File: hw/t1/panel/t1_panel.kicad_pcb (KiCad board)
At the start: 4 copper layers, 70.5 x 81 mm, 376 parts, among them J1 SFP edge (INF-8074i), J2 Rosenberger E6S20A-40MT5-Z (H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, U1 DP83TG720S-Q1 (or DP83TC812S-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, U2 STM32G031F6P6, U3 TPS62822DLC, Y1 25MHz CL8pF 2016

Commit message: t1: opens clean in KiCad 9 - schematic parity, linked footprints, check script
A KiCad 9 check (official Docker image, as a reviewer would open it) found
what KiCad 7's python and kicad-cli could not test:
- no footprint was linked to its schematic symbol: KiCad's Update PCB
  would have replaced every part. Footprints now carry /<symbol uuid>
  plus Sheetname/Sheetfile
- 140 net-name conflicts: local labels name nets /TD_P on the root sheet,
  the board says TD_P. The schematic now uses global labels
- no-connect pins are nets of their own in KiCad
  (unconnected-(REF-PIN-PadN)); the pads now carry them
- DNP/BOM flags agreed nowhere (ESD diodes, test pads): excluded from the
  BOM on both sides (KiCad 7 boards have no DNP attribute)
- back-side label was not mirrored
- the buck's footprint is gone from KiCad 9's library: vendored into
  hw/fp/sfp.pretty

Result (sh hw/check_kicad9.sh t1): DRC 0 errors / 0 unconnected, parity
clean, ERC 0 errors; the only warnings are KiCad 9's newer library copies.
Copper is unchanged (tracks, vias, pads and fills compared item by item);
gerber/CPL/BOM changes are ordering only. KiCad 7 ERC 0/0, DRC 0/0.
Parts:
- removed the U3 at (125.2, 59.3)
- removed the U3 at (125.2, 45.5)
- removed the U3 at (125.2, 31.7)
- removed the U3 at (125.2, 86.9)
- removed the U3 at (125.2, 73.1)
- added U3: TPS62822DLC, sfp:Texas_VSON-HR-8_1.5x2mm_P0.5mm, F.Cu at (125.2, 45.5)
- added U3: TPS62822DLC, sfp:Texas_VSON-HR-8_1.5x2mm_P0.5mm, F.Cu at (125.2, 59.3)
- added U3: TPS62822DLC, sfp:Texas_VSON-HR-8_1.5x2mm_P0.5mm, F.Cu at (125.2, 73.1)
- added U3: TPS62822DLC, sfp:Texas_VSON-HR-8_1.5x2mm_P0.5mm, F.Cu at (125.2, 86.9)
- added U3: TPS62822DLC, sfp:Texas_VSON-HR-8_1.5x2mm_P0.5mm, F.Cu at (125.2, 31.7)
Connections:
- J1 pad 7: (no net) -> Board_0-unconnected-(J1-RS0-Pad7)
- J1 pad 7: (no net) -> Board_3-unconnected-(J1-RS0-Pad7)
- J1 pad 7: (no net) -> Board_4-unconnected-(J1-RS0-Pad7)
- J1 pad 7: (no net) -> Board_2-unconnected-(J1-RS0-Pad7)
- J1 pad 7: (no net) -> Board_1-unconnected-(J1-RS0-Pad7)
- U1 pad 10: (no net) -> Board_3-unconnected-(U1-INH-Pad10)
- U1 pad 14: (no net) -> Board_3-unconnected-(U1-STRP_1-Pad14)
- U1 pad 15: (no net) -> Board_3-unconnected-(U1-RX_CTRL-Pad15)
- U1 pad 16: (no net) -> Board_3-unconnected-(U1-CLKOUT-Pad16)
- U1 pad 17: (no net) -> Board_3-unconnected-(U1-DNC-Pad17)
- U1 pad 18: (no net) -> Board_3-unconnected-(U1-DNC-Pad18)
- U1 pad 19: (no net) -> Board_3-unconnected-(U1-DNC-Pad19)
- U1 pad 20: (no net) -> Board_3-unconnected-(U1-DNC-Pad20)
- U1 pad 25: (no net) -> Board_3-unconnected-(U1-RX_D1-Pad25)
- U1 pad 26: (no net) -> Board_3-unconnected-(U1-RX_D0-Pad26)
- U1 pad 27: (no net) -> Board_3-unconnected-(U1-RX_CLK-Pad27)
- U1 pad 28: (no net) -> Board_3-unconnected-(U1-TX_CLK-Pad28)
- U1 pad 29: (no net) -> Board_3-unconnected-(U1-TX_CTRL-Pad29)
- U1 pad 30: (no net) -> Board_3-unconnected-(U1-TX_D3-Pad30)
- U1 pad 31: (no net) -> Board_3-unconnected-(U1-TX_D2-Pad31)
- U1 pad 6: (no net) -> Board_3-unconnected-(U1-LED_1/AUTO-Pad6)
- U1 pad 8: (no net) -> Board_3-unconnected-(U1-WAKE-Pad8)
- U1 pad 10: (no net) -> Board_1-unconnected-(U1-INH-Pad10)
- U1 pad 14: (no net) -> Board_1-unconnected-(U1-STRP_1-Pad14)
- U1 pad 15: (no net) -> Board_1-unconnected-(U1-RX_CTRL-Pad15)
- U1 pad 16: (no net) -> Board_1-unconnected-(U1-CLKOUT-Pad16)
- U1 pad 17: (no net) -> Board_1-unconnected-(U1-DNC-Pad17)
- U1 pad 18: (no net) -> Board_1-unconnected-(U1-DNC-Pad18)
- U1 pad 19: (no net) -> Board_1-unconnected-(U1-DNC-Pad19)
- U1 pad 20: (no net) -> Board_1-unconnected-(U1-DNC-Pad20)
- U1 pad 25: (no net) -> Board_1-unconnected-(U1-RX_D1-Pad25)
- U1 pad 26: (no net) -> Board_1-unconnected-(U1-RX_D0-Pad26)
- U1 pad 27: (no net) -> Board_1-unconnected-(U1-RX_CLK-Pad27)
- U1 pad 28: (no net) -> Board_1-unconnected-(U1-TX_CLK-Pad28)
- U1 pad 29: (no net) -> Board_1-unconnected-(U1-TX_CTRL-Pad29)
- U1 pad 30: (no net) -> Board_1-unconnected-(U1-TX_D3-Pad30)
- U1 pad 31: (no net) -> Board_1-unconnected-(U1-TX_D2-Pad31)
- U1 pad 6: (no net) -> Board_1-unconnected-(U1-LED_1/AUTO-Pad6)
- U1 pad 8: (no net) -> Board_1-unconnected-(U1-WAKE-Pad8)
- U1 pad 10: (no net) -> Board_4-unconnected-(U1-INH-Pad10)
- U1 pad 14: (no net) -> Board_4-unconnected-(U1-STRP_1-Pad14)
- U1 pad 15: (no net) -> Board_4-unconnected-(U1-RX_CTRL-Pad15)
- U1 pad 16: (no net) -> Board_4-unconnected-(U1-CLKOUT-Pad16)
- U1 pad 17: (no net) -> Board_4-unconnected-(U1-DNC-Pad17)
- U1 pad 18: (no net) -> Board_4-unconnected-(U1-DNC-Pad18)
- U1 pad 19: (no net) -> Board_4-unconnected-(U1-DNC-Pad19)
- U1 pad 20: (no net) -> Board_4-unconnected-(U1-DNC-Pad20)
- U1 pad 25: (no net) -> Board_4-unconnected-(U1-RX_D1-Pad25)
- U1 pad 26: (no net) -> Board_4-unconnected-(U1-RX_D0-Pad26)
- U1 pad 27: (no net) -> Board_4-unconnected-(U1-RX_CLK-Pad27)
- U1 pad 28: (no net) -> Board_4-unconnected-(U1-TX_CLK-Pad28)
- U1 pad 29: (no net) -> Board_4-unconnected-(U1-TX_CTRL-Pad29)
- U1 pad 30: (no net) -> Board_4-unconnected-(U1-TX_D3-Pad30)
- U1 pad 31: (no net) -> Board_4-unconnected-(U1-TX_D2-Pad31)
- U1 pad 6: (no net) -> Board_4-unconnected-(U1-LED_1/AUTO-Pad6)
- U1 pad 8: (no net) -> Board_4-unconnected-(U1-WAKE-Pad8)
- U1 pad 10: (no net) -> Board_0-unconnected-(U1-INH-Pad10)
- U1 pad 14: (no net) -> Board_0-unconnected-(U1-STRP_1-Pad14)
- U1 pad 15: (no net) -> Board_0-unconnected-(U1-RX_CTRL-Pad15)
- U1 pad 16: (no net) -> Board_0-unconnected-(U1-CLKOUT-Pad16)
- U1 pad 17: (no net) -> Board_0-unconnected-(U1-DNC-Pad17)
- U1 pad 18: (no net) -> Board_0-unconnected-(U1-DNC-Pad18)
- U1 pad 19: (no net) -> Board_0-unconnected-(U1-DNC-Pad19)
- U1 pad 20: (no net) -> Board_0-unconnected-(U1-DNC-Pad20)
- U1 pad 25: (no net) -> Board_0-unconnected-(U1-RX_D1-Pad25)
- U1 pad 26: (no net) -> Board_0-unconnected-(U1-RX_D0-Pad26)
- U1 pad 27: (no net) -> Board_0-unconnected-(U1-RX_CLK-Pad27)
- U1 pad 28: (no net) -> Board_0-unconnected-(U1-TX_CLK-Pad28)
- U1 pad 29: (no net) -> Board_0-unconnected-(U1-TX_CTRL-Pad29)
- U1 pad 30: (no net) -> Board_0-unconnected-(U1-TX_D3-Pad30)
- U1 pad 31: (no net) -> Board_0-unconnected-(U1-TX_D2-Pad31)
- U1 pad 6: (no net) -> Board_0-unconnected-(U1-LED_1/AUTO-Pad6)
- U1 pad 8: (no net) -> Board_0-unconnected-(U1-WAKE-Pad8)
- U1 pad 10: (no net) -> Board_2-unconnected-(U1-INH-Pad10)
- U1 pad 14: (no net) -> Board_2-unconnected-(U1-STRP_1-Pad14)
- U1 pad 15: (no net) -> Board_2-unconnected-(U1-RX_CTRL-Pad15)
- U1 pad 16: (no net) -> Board_2-unconnected-(U1-CLKOUT-Pad16)
- U1 pad 17: (no net) -> Board_2-unconnected-(U1-DNC-Pad17)
- U1 pad 18: (no net) -> Board_2-unconnected-(U1-DNC-Pad18)
- U1 pad 19: (no net) -> Board_2-unconnected-(U1-DNC-Pad19)
- U1 pad 20: (no net) -> Board_2-unconnected-(U1-DNC-Pad20)
- U1 pad 25: (no net) -> Board_2-unconnected-(U1-RX_D1-Pad25)
- U1 pad 26: (no net) -> Board_2-unconnected-(U1-RX_D0-Pad26)
- U1 pad 27: (no net) -> Board_2-unconnected-(U1-RX_CLK-Pad27)
- U1 pad 28: (no net) -> Board_2-unconnected-(U1-TX_CLK-Pad28)
- U1 pad 29: (no net) -> Board_2-unconnected-(U1-TX_CTRL-Pad29)
- U1 pad 30: (no net) -> Board_2-unconnected-(U1-TX_D3-Pad30)
- U1 pad 31: (no net) -> Board_2-unconnected-(U1-TX_D2-Pad31)
- U1 pad 6: (no net) -> Board_2-unconnected-(U1-LED_1/AUTO-Pad6)
- U1 pad 8: (no net) -> Board_2-unconnected-(U1-WAKE-Pad8)
- U2 pad 14: (no net) -> Board_0-unconnected-(U2-PA7-Pad14)
- U2 pad 15: (no net) -> Board_0-unconnected-(U2-PB0/PB1/PB2/PA8-Pad15)
- U2 pad 16: (no net) -> Board_0-unconnected-(U2-PA11/PA9-Pad16)
- U2 pad 17: (no net) -> Board_0-unconnected-(U2-PA12/PA10-Pad17)
- U2 pad 2: (no net) -> Board_0-unconnected-(U2-PC14/PB9-Pad2)
- U2 pad 3: (no net) -> Board_0-unconnected-(U2-PC15-Pad3)
- U2 pad 14: (no net) -> Board_4-unconnected-(U2-PA7-Pad14)
- U2 pad 15: (no net) -> Board_4-unconnected-(U2-PB0/PB1/PB2/PA8-Pad15)
- U2 pad 16: (no net) -> Board_4-unconnected-(U2-PA11/PA9-Pad16)
- U2 pad 17: (no net) -> Board_4-unconnected-(U2-PA12/PA10-Pad17)
- U2 pad 2: (no net) -> Board_4-unconnected-(U2-PC14/PB9-Pad2)
- U2 pad 3: (no net) -> Board_4-unconnected-(U2-PC15-Pad3)
- U2 pad 14: (no net) -> Board_2-unconnected-(U2-PA7-Pad14)
- U2 pad 15: (no net) -> Board_2-unconnected-(U2-PB0/PB1/PB2/PA8-Pad15)
- U2 pad 16: (no net) -> Board_2-unconnected-(U2-PA11/PA9-Pad16)
- U2 pad 17: (no net) -> Board_2-unconnected-(U2-PA12/PA10-Pad17)
- U2 pad 2: (no net) -> Board_2-unconnected-(U2-PC14/PB9-Pad2)
- U2 pad 3: (no net) -> Board_2-unconnected-(U2-PC15-Pad3)
- U2 pad 14: (no net) -> Board_3-unconnected-(U2-PA7-Pad14)
- U2 pad 15: (no net) -> Board_3-unconnected-(U2-PB0/PB1/PB2/PA8-Pad15)
- U2 pad 16: (no net) -> Board_3-unconnected-(U2-PA11/PA9-Pad16)
- U2 pad 17: (no net) -> Board_3-unconnected-(U2-PA12/PA10-Pad17)
- U2 pad 2: (no net) -> Board_3-unconnected-(U2-PC14/PB9-Pad2)
- U2 pad 3: (no net) -> Board_3-unconnected-(U2-PC15-Pad3)
- U2 pad 14: (no net) -> Board_1-unconnected-(U2-PA7-Pad14)
- U2 pad 15: (no net) -> Board_1-unconnected-(U2-PB0/PB1/PB2/PA8-Pad15)
- U2 pad 16: (no net) -> Board_1-unconnected-(U2-PA11/PA9-Pad16)
- U2 pad 17: (no net) -> Board_1-unconnected-(U2-PA12/PA10-Pad17)
- U2 pad 2: (no net) -> Board_1-unconnected-(U2-PC14/PB9-Pad2)
- U2 pad 3: (no net) -> Board_1-unconnected-(U2-PC15-Pad3)

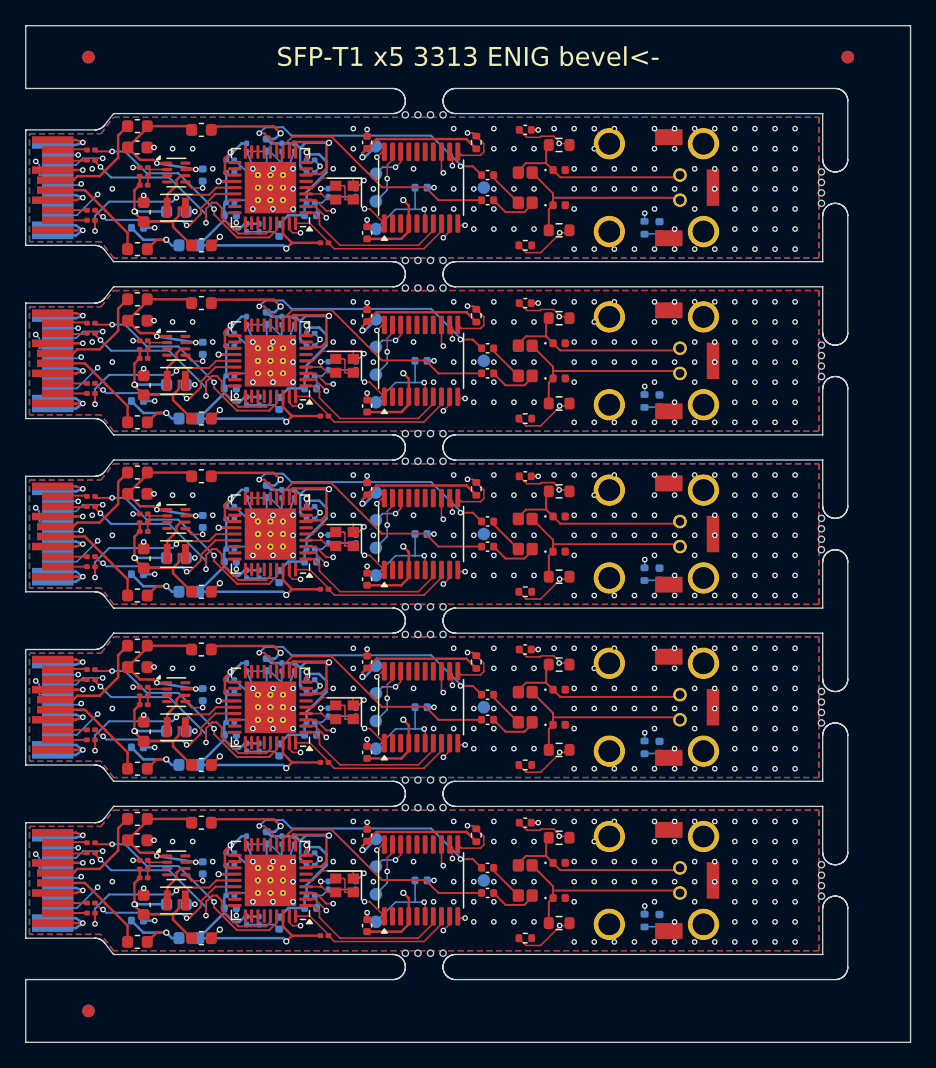
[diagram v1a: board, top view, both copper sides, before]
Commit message: t1: design-review fixes - coupled pairs by hand, F/GND/GND/B, load switch, two BOMs, CI
- every SGMII/MDI pair laid coupled (0.114/0.152, ~100 ohm diff) on one layer
  with matched vias; router does the slow nets only. Worst skew 1.08 mm (SG_RX)
- In2 is GND; slow signals may cross it except under the bottom-side pair
- SGMII lanes laid straight, polarity inverted in the PHY by the firmware
  (SGMII_CTRL_1 bits 7/8, TG720 and TC812)
- TPS22918 load switch on the 3.3 V entry (~3.6 ms soft start)
- 0.6 mm no-copper strip along every edge (mouse bites); escapes where it
  closed the router's way (U4 ON, MDC/INT/RST, VDD1P0, MCU GND, XO)
- jlc/bom.csv + cpl.csv replaced by bom/cpl-tg720 and bom/cpl-tc812
- fab/t1-1to1.pdf for the H-MTD print check
- KiCad 9: DRC 0, parity clean, ERC clean; only lib-revision warnings pass
- GitHub Actions: KiCad 9 check, firmware (4 variants, no warnings), gateware
- root README rewritten (11.8 mm body, current status, hardware-only checks)
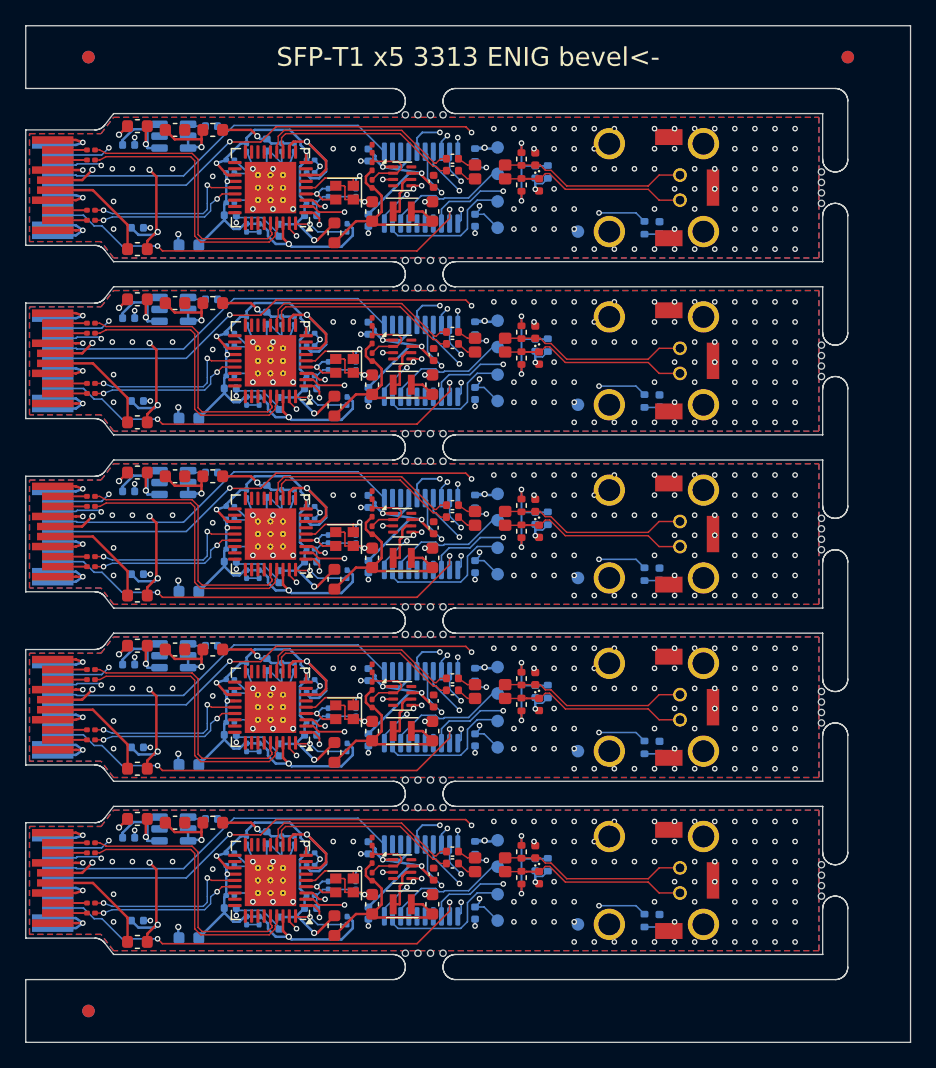
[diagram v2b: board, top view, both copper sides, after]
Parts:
- removed the C1 at (122.2, 43.5)
- removed the C1 at (122.2, 84.9)
- removed the C1 at (122.2, 57.3)
- removed the C1 at (122.2, 29.7)
- removed the C1 at (122.2, 71.1)
- removed the C26 at (127.3, 31.9)
- removed the C26 at (127.3, 45.7)
- removed the C26 at (127.3, 73.3)
- removed the C26 at (127.3, 59.5)
- removed the C26 at (127.3, 87.1)
- removed the C27 at (122.7, 90.0)
- removed the C27 at (122.7, 76.2)
- removed the C27 at (122.7, 34.9)
- removed the C27 at (122.7, 48.6)
- removed the C27 at (122.7, 62.5)
- removed the C28 at (125.2, 62.4)
- removed the C28 at (125.2, 48.6)
- removed the C28 at (125.2, 34.8)
- removed the C28 at (125.2, 76.2)
- removed the C28 at (125.2, 90.0)
- removed the C29 at (122.7, 59.6)
- removed the C29 at (122.7, 73.4)
- removed the C29 at (122.7, 87.2)
- removed the C29 at (122.7, 32.0)
- removed the C29 at (122.7, 45.8)
- removed the C30 at (140.4, 56.9)
- removed the C30 at (140.4, 43.1)
- removed the C30 at (140.4, 29.3)
- removed the C30 at (140.4, 70.7)
- removed the C30 at (140.4, 84.5)
- removed the C31 at (140.4, 50.3)
- removed the C31 at (140.4, 91.7)
- removed the C31 at (140.4, 77.9)
- removed the C31 at (140.4, 64.1)
- removed the C31 at (140.4, 36.5)
- removed the C32 at (144.8, 46.7)
- removed the C32 at (144.8, 88.1)
- removed the C32 at (144.8, 74.3)
- removed the C32 at (144.8, 32.9)
- removed the C32 at (144.8, 60.5)
- removed the C33 at (150.1, 87.1)
- removed the C33 at (150.1, 59.5)
- removed the C33 at (150.1, 73.3)
- removed the C33 at (150.1, 31.9)
- removed the C33 at (150.1, 45.7)
- removed the C34 at (150.1, 33.9)
- removed the C34 at (150.1, 61.5)
- removed the C34 at (150.1, 47.7)
- removed the C34 at (150.1, 89.1)
- removed the C34 at (150.1, 75.3)
- removed the C35 at (153.1, 28.3)
- removed the C35 at (153.1, 83.5)
- removed the C35 at (153.1, 55.9)
- removed the C35 at (153.1, 69.7)
- removed the C35 at (153.1, 42.1)
- removed the D2 at (155.8, 72.9)
- removed the D2 at (155.8, 31.5)
- removed the D2 at (155.8, 86.7)
- removed the D2 at (155.8, 45.3)
- removed the D2 at (155.8, 59.1)
- removed the D3 at (155.8, 75.7)
- removed the D3 at (155.8, 34.3)
- removed the D3 at (155.8, 48.1)
- removed the D3 at (155.8, 89.5)
- removed the D3 at (155.8, 61.9)
- removed the FB3 at (127.2, 37.5)
- removed the FB3 at (127.2, 92.7)
- removed the FB3 at (127.2, 78.9)
- removed the FB3 at (127.2, 51.3)
- removed the FB3 at (127.2, 65.1)
- removed the FB4 at (127.2, 69.7)
- removed the FB4 at (127.2, 55.9)
- removed the FB4 at (127.2, 42.1)
- removed the FB4 at (127.2, 83.5)
- removed the FB4 at (127.2, 28.3)
- removed the L1 at (125.2, 75.9)
- removed the L1 at (125.2, 34.5)
- removed the L1 at (125.2, 62.1)
- removed the L1 at (125.2, 48.3)
- removed the L1 at (125.2, 89.7)
- removed the L2 at (153.1, 60.5)
- removed the L2 at (153.1, 32.9)
- removed the L2 at (153.1, 88.1)
- removed the L2 at (153.1, 74.3)
- removed the L2 at (153.1, 46.7)
- removed the R1 at (137.1, 64.9)
- removed the R1 at (137.1, 78.7)
- removed the R1 at (137.1, 37.3)
- removed the R1 at (137.1, 51.1)
- removed the R1 at (137.1, 92.5)
- removed the R3 at (122.7, 87.9)
- removed the R3 at (122.7, 74.1)
- removed the R3 at (122.7, 46.5)
- removed the R3 at (122.7, 60.3)
- removed the R3 at (122.7, 32.7)
- removed the R4 at (122.7, 72.7)
- removed the R4 at (122.7, 86.5)
- removed the R4 at (122.7, 58.9)
- removed the R4 at (122.7, 31.3)
- removed the R4 at (122.7, 45.1)
- removed the R5 at (149.2, 29.3)
- removed the R5 at (149.2, 56.9)
- removed the R5 at (149.2, 70.7)
- removed the R5 at (149.2, 43.1)
- removed the R5 at (149.2, 84.5)
- removed the R6 at (155.8, 57.1)
- removed the R6 at (155.8, 43.3)
- removed the R6 at (155.8, 84.7)
- removed the R6 at (155.8, 70.9)
- removed the R6 at (155.8, 29.5)
- removed the R7 at (155.8, 91.5)
- removed the R7 at (155.8, 50.1)
- removed the R7 at (155.8, 36.3)
- removed the R7 at (155.8, 77.7)
- removed the R7 at (155.8, 63.9)
- removed the R8 at (153.1, 37.5)
- removed the R8 at (153.1, 78.9)
- removed the R8 at (153.1, 65.1)
- removed the R8 at (153.1, 92.7)
- removed the R8 at (153.1, 51.3)
- removed the TP1 at (141.2, 43.4)
- removed the TP1 at (141.2, 57.2)
- removed the TP1 at (141.2, 84.8)
- removed the TP1 at (141.2, 29.6)
- removed the TP1 at (141.2, 71.0)
- removed the TP2 at (141.2, 31.8)
- removed the TP2 at (141.2, 73.2)
- removed the TP2 at (141.2, 59.4)
- removed the TP2 at (141.2, 45.6)
- removed the TP2 at (141.2, 87.0)
- removed the TP3 at (141.2, 75.4)
- removed the TP3 at (141.2, 34.0)
- removed the TP3 at (141.2, 89.2)
- removed the TP3 at (141.2, 61.6)
- removed the TP3 at (141.2, 47.8)
- removed the TP4 at (141.2, 91.4)
- removed the TP4 at (141.2, 50.0)
- removed the TP4 at (141.2, 77.6)
- removed the TP4 at (141.2, 63.8)
- removed the TP4 at (141.2, 36.2)
- removed the TP5 at (149.8, 60.5)
- removed the TP5 at (149.8, 46.7)
- removed the TP5 at (149.8, 32.9)
- removed the TP5 at (149.8, 74.3)
- removed the TP5 at (149.8, 88.1)
- removed the U3 at (125.2, 45.5)
- removed the U3 at (125.2, 59.3)
- removed the U3 at (125.2, 73.1)
- removed the U3 at (125.2, 86.9)
- removed the U3 at (125.2, 31.7)
- added C1: 1uF, Capacitor_SMD:C_0402_1005Metric, B.Cu at (121.5, 70.9)
- added C1: 1uF, Capacitor_SMD:C_0402_1005Metric, B.Cu at (121.5, 43.3)
- added C1: 1uF, Capacitor_SMD:C_0402_1005Metric, B.Cu at (121.5, 57.1)
- added C1: 1uF, Capacitor_SMD:C_0402_1005Metric, B.Cu at (121.5, 84.7)
- added C1: 1uF, Capacitor_SMD:C_0402_1005Metric, B.Cu at (121.5, 29.5)
- added C26: 4.7uF, Capacitor_SMD:C_0402_1005Metric, F.Cu at (145.8, 60.0)
- added C26: 4.7uF, Capacitor_SMD:C_0402_1005Metric, F.Cu at (145.8, 87.6)
- added C26: 4.7uF, Capacitor_SMD:C_0402_1005Metric, F.Cu at (145.8, 73.8)
- added C26: 4.7uF, Capacitor_SMD:C_0402_1005Metric, F.Cu at (145.8, 46.2)
- added C26: 4.7uF, Capacitor_SMD:C_0402_1005Metric, F.Cu at (145.8, 32.4)
- added C27: 10uF, Capacitor_SMD:C_0603_1608Metric, F.Cu at (140.8, 76.2)
- added C27: 10uF, Capacitor_SMD:C_0603_1608Metric, F.Cu at (140.8, 62.4)
- added C27: 10uF, Capacitor_SMD:C_0603_1608Metric, F.Cu at (140.8, 34.8)
- added C27: 10uF, Capacitor_SMD:C_0603_1608Metric, F.Cu at (140.8, 90.0)
- added C27: 10uF, Capacitor_SMD:C_0603_1608Metric, F.Cu at (140.8, 48.6)
- added C28: 10uF, Capacitor_SMD:C_0603_1608Metric, F.Cu at (145.7, 76.2)
- added C28: 10uF, Capacitor_SMD:C_0603_1608Metric, F.Cu at (145.7, 90.0)
- added C28: 10uF, Capacitor_SMD:C_0603_1608Metric, F.Cu at (145.7, 34.8)
- added C28: 10uF, Capacitor_SMD:C_0603_1608Metric, F.Cu at (145.7, 48.6)
- added C28: 10uF, Capacitor_SMD:C_0603_1608Metric, F.Cu at (145.7, 62.4)
- added C29: 120pF, Capacitor_SMD:C_0201_0603Metric, F.Cu at (140.8, 31.2)
- added C29: 120pF, Capacitor_SMD:C_0201_0603Metric, F.Cu at (140.8, 86.4)
- added C29: 120pF, Capacitor_SMD:C_0201_0603Metric, F.Cu at (140.8, 72.6)
- added C29: 120pF, Capacitor_SMD:C_0201_0603Metric, F.Cu at (140.8, 45.0)
- added C29: 120pF, Capacitor_SMD:C_0201_0603Metric, F.Cu at (140.8, 58.8)
- added C30: 100nF, Capacitor_SMD:C_0402_1005Metric, B.Cu at (140.6, 85.5)
- added C30: 100nF, Capacitor_SMD:C_0402_1005Metric, B.Cu at (140.6, 44.1)
- added C30: 100nF, Capacitor_SMD:C_0402_1005Metric, B.Cu at (140.6, 57.9)
- added C30: 100nF, Capacitor_SMD:C_0402_1005Metric, B.Cu at (140.6, 30.3)
- added C30: 100nF, Capacitor_SMD:C_0402_1005Metric, B.Cu at (140.6, 71.7)
- added C31: 1uF, Capacitor_SMD:C_0402_1005Metric, B.Cu at (140.6, 63.1)
- added C31: 1uF, Capacitor_SMD:C_0402_1005Metric, B.Cu at (140.6, 49.3)
- added C31: 1uF, Capacitor_SMD:C_0402_1005Metric, B.Cu at (140.6, 76.9)
- added C31: 1uF, Capacitor_SMD:C_0402_1005Metric, B.Cu at (140.6, 35.5)
- added C31: 1uF, Capacitor_SMD:C_0402_1005Metric, B.Cu at (140.6, 90.7)
- added C32: 100nF, Capacitor_SMD:C_0402_1005Metric, B.Cu at (149.1, 63.1)
- added C32: 100nF, Capacitor_SMD:C_0402_1005Metric, B.Cu at (149.1, 76.9)
- added C32: 100nF, Capacitor_SMD:C_0402_1005Metric, B.Cu at (149.1, 49.3)
- added C32: 100nF, Capacitor_SMD:C_0402_1005Metric, B.Cu at (149.1, 90.7)
- added C32: 100nF, Capacitor_SMD:C_0402_1005Metric, B.Cu at (149.1, 35.5)
- added C33: 100nF, Capacitor_SMD:C_0402_1005Metric, F.Cu at (147.2, 44.4)
- added C33: 100nF, Capacitor_SMD:C_0402_1005Metric, F.Cu at (147.2, 85.8)
- added C33: 100nF, Capacitor_SMD:C_0402_1005Metric, F.Cu at (147.2, 30.6)
- added C33: 100nF, Capacitor_SMD:C_0402_1005Metric, F.Cu at (147.2, 72.0)
- added C33: 100nF, Capacitor_SMD:C_0402_1005Metric, F.Cu at (147.2, 58.2)
- added C34: 100nF, Capacitor_SMD:C_0402_1005Metric, F.Cu at (147.2, 59.1)
- added C34: 100nF, Capacitor_SMD:C_0402_1005Metric, F.Cu at (147.2, 45.4)
- added C34: 100nF, Capacitor_SMD:C_0402_1005Metric, F.Cu at (147.2, 31.6)
- added C34: 100nF, Capacitor_SMD:C_0402_1005Metric, F.Cu at (147.2, 73.0)
- added C34: 100nF, Capacitor_SMD:C_0402_1005Metric, F.Cu at (147.2, 86.8)
- added C35: 4.7nF, Capacitor_SMD:C_0402_1005Metric, B.Cu at (153.8, 86.8)
- added C35: 4.7nF, Capacitor_SMD:C_0402_1005Metric, B.Cu at (153.8, 73.0)
- added C35: 4.7nF, Capacitor_SMD:C_0402_1005Metric, B.Cu at (153.8, 45.5)
- added C35: 4.7nF, Capacitor_SMD:C_0402_1005Metric, B.Cu at (153.8, 59.2)
- added C35: 4.7nF, Capacitor_SMD:C_0402_1005Metric, B.Cu at (153.8, 31.6)
- added C36: 2.2nF, Capacitor_SMD:C_0402_1005Metric, B.Cu at (128.1, 69.4)
- added C36: 2.2nF, Capacitor_SMD:C_0402_1005Metric, B.Cu at (128.1, 55.6)
- added C36: 2.2nF, Capacitor_SMD:C_0402_1005Metric, B.Cu at (128.1, 83.2)
- added C36: 2.2nF, Capacitor_SMD:C_0402_1005Metric, B.Cu at (128.1, 28.0)
- added C36: 2.2nF, Capacitor_SMD:C_0402_1005Metric, B.Cu at (128.1, 41.8)
- added C37: 10uF, Capacitor_SMD:C_0603_1608Metric, F.Cu at (125.2, 42.1)
- added C37: 10uF, Capacitor_SMD:C_0603_1608Metric, F.Cu at (125.2, 55.9)
- added C37: 10uF, Capacitor_SMD:C_0603_1608Metric, F.Cu at (125.2, 83.5)
- added C37: 10uF, Capacitor_SMD:C_0603_1608Metric, F.Cu at (125.2, 69.7)
- added C37: 10uF, Capacitor_SMD:C_0603_1608Metric, F.Cu at (125.2, 28.3)
- added D2: ESD (DNP), Diode_SMD:D_0402_1005Metric, F.Cu at (153.8, 72.0)
- added D2: ESD (DNP), Diode_SMD:D_0402_1005Metric, F.Cu at (153.8, 30.6)
- added D2: ESD (DNP), Diode_SMD:D_0402_1005Metric, F.Cu at (153.8, 58.2)
- added D2: ESD (DNP), Diode_SMD:D_0402_1005Metric, F.Cu at (153.8, 85.8)
- added D2: ESD (DNP), Diode_SMD:D_0402_1005Metric, F.Cu at (153.8, 44.4)
- added D3: ESD (DNP), Diode_SMD:D_0402_1005Metric, F.Cu at (154.2, 60.3)
- added D3: ESD (DNP), Diode_SMD:D_0402_1005Metric, F.Cu at (154.2, 87.9)
- added D3: ESD (DNP), Diode_SMD:D_0402_1005Metric, F.Cu at (154.2, 32.7)
- added D3: ESD (DNP), Diode_SMD:D_0402_1005Metric, F.Cu at (154.2, 46.5)
- added D3: ESD (DNP), Diode_SMD:D_0402_1005Metric, F.Cu at (154.2, 74.1)
- added FB3: BLM18KG601SH1 (DNP for DP83TC812), Inductor_SMD:L_0603_1608Metric, F.Cu at (137.8, 64.1)
- added FB3: BLM18KG601SH1 (DNP for DP83TC812), Inductor_SMD:L_0603_1608Metric, F.Cu at (137.8, 50.3)
- added FB3: BLM18KG601SH1 (DNP for DP83TC812), Inductor_SMD:L_0603_1608Metric, F.Cu at (137.8, 36.5)
- added FB3: BLM18KG601SH1 (DNP for DP83TC812), Inductor_SMD:L_0603_1608Metric, F.Cu at (137.8, 91.7)
- added FB3: BLM18KG601SH1 (DNP for DP83TC812), Inductor_SMD:L_0603_1608Metric, F.Cu at (137.8, 77.9)
- added FB4: BLM18KG601SH1, Inductor_SMD:L_0603_1608Metric, F.Cu at (128.2, 83.5)
- added FB4: BLM18KG601SH1, Inductor_SMD:L_0603_1608Metric, F.Cu at (128.2, 28.3)
- added FB4: BLM18KG601SH1, Inductor_SMD:L_0603_1608Metric, F.Cu at (128.2, 69.7)
- added FB4: BLM18KG601SH1, Inductor_SMD:L_0603_1608Metric, F.Cu at (128.2, 55.9)
- added FB4: BLM18KG601SH1, Inductor_SMD:L_0603_1608Metric, F.Cu at (128.2, 42.1)
- added L1: 470nH DFE201610E-R47M, Inductor_SMD:L_Murata_DFE201610P, F.Cu at (143.2, 62.4)
- added L1: 470nH DFE201610E-R47M, Inductor_SMD:L_Murata_DFE201610P, F.Cu at (143.2, 90.0)
- added L1: 470nH DFE201610E-R47M, Inductor_SMD:L_Murata_DFE201610P, F.Cu at (143.2, 76.2)
- added L1: 470nH DFE201610E-R47M, Inductor_SMD:L_Murata_DFE201610P, F.Cu at (143.2, 34.8)
- added L1: 470nH DFE201610E-R47M, Inductor_SMD:L_Murata_DFE201610P, F.Cu at (143.2, 48.6)
- added L2: DLW32MH101XT2, sfp:L_CommonMode_3225, F.Cu at (150.2, 86.8)
- added L2: DLW32MH101XT2, sfp:L_CommonMode_3225, F.Cu at (150.2, 45.5)
- added L2: DLW32MH101XT2, sfp:L_CommonMode_3225, F.Cu at (150.2, 73.0)
- added L2: DLW32MH101XT2, sfp:L_CommonMode_3225, F.Cu at (150.2, 31.6)
- added L2: DLW32MH101XT2, sfp:L_CommonMode_3225, F.Cu at (150.2, 59.2)
- added R1: 2.2k, Resistor_SMD:R_0201_0603Metric, B.Cu at (138.8, 36.1)
- added R1: 2.2k, Resistor_SMD:R_0201_0603Metric, B.Cu at (138.8, 49.9)
- added R1: 2.2k, Resistor_SMD:R_0201_0603Metric, B.Cu at (138.8, 63.7)
- added R1: 2.2k, Resistor_SMD:R_0201_0603Metric, B.Cu at (138.8, 91.3)
- added R1: 2.2k, Resistor_SMD:R_0201_0603Metric, B.Cu at (138.8, 77.5)
- added R3: 66.5k 1%, Resistor_SMD:R_0201_0603Metric, F.Cu at (140.8, 32.6)
- added R3: 66.5k 1%, Resistor_SMD:R_0201_0603Metric, F.Cu at (140.8, 87.8)
- added R3: 66.5k 1%, Resistor_SMD:R_0201_0603Metric, F.Cu at (140.8, 74.0)
- added R3: 66.5k 1%, Resistor_SMD:R_0201_0603Metric, F.Cu at (140.8, 46.4)
- added R3: 66.5k 1%, Resistor_SMD:R_0201_0603Metric, F.Cu at (140.8, 60.2)
- added R4: 100k 1%, Resistor_SMD:R_0201_0603Metric, F.Cu at (140.8, 71.2)
- added R4: 100k 1%, Resistor_SMD:R_0201_0603Metric, F.Cu at (140.8, 85.0)
- added R4: 100k 1%, Resistor_SMD:R_0201_0603Metric, F.Cu at (140.8, 29.8)
- added R4: 100k 1%, Resistor_SMD:R_0201_0603Metric, F.Cu at (140.8, 57.4)
- added R4: 100k 1%, Resistor_SMD:R_0201_0603Metric, F.Cu at (140.8, 43.6)
- added R5: 10k, Resistor_SMD:R_0402_1005Metric, B.Cu at (149.1, 85.5)
- added R5: 10k, Resistor_SMD:R_0402_1005Metric, B.Cu at (149.1, 71.7)
- added R5: 10k, Resistor_SMD:R_0402_1005Metric, B.Cu at (149.1, 30.3)
- added R5: 10k, Resistor_SMD:R_0402_1005Metric, B.Cu at (149.1, 44.1)
- added R5: 10k, Resistor_SMD:R_0402_1005Metric, B.Cu at (149.1, 57.9)
- added R6: 1k 1%, Resistor_SMD:R_0402_1005Metric, F.Cu at (152.8, 58.2)
- added R6: 1k 1%, Resistor_SMD:R_0402_1005Metric, F.Cu at (152.8, 85.8)
- added R6: 1k 1%, Resistor_SMD:R_0402_1005Metric, F.Cu at (152.8, 72.0)
- added R6: 1k 1%, Resistor_SMD:R_0402_1005Metric, F.Cu at (152.8, 30.6)
- added R6: 1k 1%, Resistor_SMD:R_0402_1005Metric, F.Cu at (152.8, 44.4)
- added R7: 1k 1%, Resistor_SMD:R_0402_1005Metric, F.Cu at (152.8, 87.9)
- added R7: 1k 1%, Resistor_SMD:R_0402_1005Metric, F.Cu at (152.8, 60.3)
- added R7: 1k 1%, Resistor_SMD:R_0402_1005Metric, F.Cu at (152.8, 46.5)
- added R7: 1k 1%, Resistor_SMD:R_0402_1005Metric, F.Cu at (152.8, 32.7)
- added R7: 1k 1%, Resistor_SMD:R_0402_1005Metric, F.Cu at (152.8, 74.1)
- added R8: 100k, Resistor_SMD:R_0402_1005Metric, B.Cu at (154.8, 45.5)
- added R8: 100k, Resistor_SMD:R_0402_1005Metric, B.Cu at (154.8, 86.8)
- added R8: 100k, Resistor_SMD:R_0402_1005Metric, B.Cu at (154.8, 31.6)
- added R8: 100k, Resistor_SMD:R_0402_1005Metric, B.Cu at (154.8, 73.0)
- added R8: 100k, Resistor_SMD:R_0402_1005Metric, B.Cu at (154.8, 59.2)
- added TP1: +3V3, TestPoint:TestPoint_Pad_D1.0mm, B.Cu at (150.8, 71.1)
- added TP1: +3V3, TestPoint:TestPoint_Pad_D1.0mm, B.Cu at (150.8, 84.9)
- added TP1: +3V3, TestPoint:TestPoint_Pad_D1.0mm, B.Cu at (150.8, 43.5)
- added TP1: +3V3, TestPoint:TestPoint_Pad_D1.0mm, B.Cu at (150.8, 57.3)
- added TP1: +3V3, TestPoint:TestPoint_Pad_D1.0mm, B.Cu at (150.8, 29.7)
- added TP2: SWDIO, TestPoint:TestPoint_Pad_D1.0mm, B.Cu at (150.8, 31.8)
- added TP2: SWDIO, TestPoint:TestPoint_Pad_D1.0mm, B.Cu at (150.8, 59.4)
- added TP2: SWDIO, TestPoint:TestPoint_Pad_D1.0mm, B.Cu at (150.8, 87.0)
- added TP2: SWDIO, TestPoint:TestPoint_Pad_D1.0mm, B.Cu at (150.8, 45.6)
- added TP2: SWDIO, TestPoint:TestPoint_Pad_D1.0mm, B.Cu at (150.8, 73.2)
- added TP3: SWCLK, TestPoint:TestPoint_Pad_D1.0mm, B.Cu at (150.8, 75.4)
- added TP3: SWCLK, TestPoint:TestPoint_Pad_D1.0mm, B.Cu at (150.8, 89.2)
- added TP3: SWCLK, TestPoint:TestPoint_Pad_D1.0mm, B.Cu at (150.8, 47.8)
- added TP3: SWCLK, TestPoint:TestPoint_Pad_D1.0mm, B.Cu at (150.8, 61.6)
- added TP3: SWCLK, TestPoint:TestPoint_Pad_D1.0mm, B.Cu at (150.8, 34.0)
- added TP4: NRST, TestPoint:TestPoint_Pad_D1.0mm, B.Cu at (150.8, 77.5)
- added TP4: NRST, TestPoint:TestPoint_Pad_D1.0mm, B.Cu at (150.8, 63.7)
- added TP4: NRST, TestPoint:TestPoint_Pad_D1.0mm, B.Cu at (150.8, 91.3)
- added TP4: NRST, TestPoint:TestPoint_Pad_D1.0mm, B.Cu at (150.8, 49.9)
- added TP4: NRST, TestPoint:TestPoint_Pad_D1.0mm, B.Cu at (150.8, 36.1)
- added TP5: GND, TestPoint:TestPoint_Pad_D1.0mm, B.Cu at (157.2, 91.6)
- added TP5: GND, TestPoint:TestPoint_Pad_D1.0mm, B.Cu at (157.2, 77.8)
- added TP5: GND, TestPoint:TestPoint_Pad_D1.0mm, B.Cu at (157.2, 50.2)
- added TP5: GND, TestPoint:TestPoint_Pad_D1.0mm, B.Cu at (157.2, 64.0)
- added TP5: GND, TestPoint:TestPoint_Pad_D1.0mm, B.Cu at (157.2, 36.4)
- added U3: TPS62822DLC, sfp:Texas_VSON-HR-8_1.5x2mm_P0.5mm, F.Cu at (143.2, 32.0)
- added U3: TPS62822DLC, sfp:Texas_VSON-HR-8_1.5x2mm_P0.5mm, F.Cu at (143.2, 87.2)
- added U3: TPS62822DLC, sfp:Texas_VSON-HR-8_1.5x2mm_P0.5mm, F.Cu at (143.2, 45.8)
- added U3: TPS62822DLC, sfp:Texas_VSON-HR-8_1.5x2mm_P0.5mm, F.Cu at (143.2, 73.4)
- added U3: TPS62822DLC, sfp:Texas_VSON-HR-8_1.5x2mm_P0.5mm, F.Cu at (143.2, 59.6)
- added U4: TPS22918DBVR, Package_TO_SOT_SMD:SOT-23-6, B.Cu at (125.0, 28.8)
- added U4: TPS22918DBVR, Package_TO_SOT_SMD:SOT-23-6, B.Cu at (125.0, 70.2)
- added U4: TPS22918DBVR, Package_TO_SOT_SMD:SOT-23-6, B.Cu at (125.0, 84.0)
- added U4: TPS22918DBVR, Package_TO_SOT_SMD:SOT-23-6, B.Cu at (125.0, 56.4)
- added U4: TPS22918DBVR, Package_TO_SOT_SMD:SOT-23-6, B.Cu at (125.0, 42.6)
- U2 (x5): moved to B.Cu
- turned U2 to -90 degrees (x5)
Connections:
- C2 pad 1: Board_2-+3V3 -> Board_2-VIN_RAW
- C2 pad 1: Board_1-+3V3 -> Board_1-VIN_RAW
- C2 pad 1: Board_3-+3V3 -> Board_3-VIN_RAW
- C2 pad 1: Board_0-+3V3 -> Board_0-VIN_RAW
- C2 pad 1: Board_4-+3V3 -> Board_4-VIN_RAW
- C3 pad 2: Board_2-SG_TX_P -> Board_2-SG_TX_N
- C3 pad 2: Board_4-SG_TX_P -> Board_4-SG_TX_N
- C3 pad 2: Board_1-SG_TX_P -> Board_1-SG_TX_N
- C3 pad 2: Board_3-SG_TX_P -> Board_3-SG_TX_N
- C3 pad 2: Board_0-SG_TX_P -> Board_0-SG_TX_N
- C4 pad 2: Board_4-SG_TX_N -> Board_4-SG_TX_P
- C4 pad 2: Board_2-SG_TX_N -> Board_2-SG_TX_P
- C4 pad 2: Board_1-SG_TX_N -> Board_1-SG_TX_P
- C4 pad 2: Board_0-SG_TX_N -> Board_0-SG_TX_P
- C4 pad 2: Board_3-SG_TX_N -> Board_3-SG_TX_P
- C5 pad 2: Board_2-SG_RX_P -> Board_2-SG_RX_N
- C5 pad 2: Board_1-SG_RX_P -> Board_1-SG_RX_N
- C5 pad 2: Board_0-SG_RX_P -> Board_0-SG_RX_N
- C5 pad 2: Board_4-SG_RX_P -> Board_4-SG_RX_N
- C5 pad 2: Board_3-SG_RX_P -> Board_3-SG_RX_N
- C6 pad 2: Board_4-SG_RX_N -> Board_4-SG_RX_P
- C6 pad 2: Board_3-SG_RX_N -> Board_3-SG_RX_P
- C6 pad 2: Board_1-SG_RX_N -> Board_1-SG_RX_P
- C6 pad 2: Board_0-SG_RX_N -> Board_0-SG_RX_P
- C6 pad 2: Board_2-SG_RX_N -> Board_2-SG_RX_P
- FB1 pad 2: Board_4-+3V3 -> Board_4-VIN_RAW
- FB1 pad 2: Board_3-+3V3 -> Board_3-VIN_RAW
- FB1 pad 2: Board_1-+3V3 -> Board_1-VIN_RAW
- FB1 pad 2: Board_2-+3V3 -> Board_2-VIN_RAW
- FB1 pad 2: Board_0-+3V3 -> Board_0-VIN_RAW
- FB2 pad 2: Board_3-+3V3 -> Board_3-VIN_RAW
- FB2 pad 2: Board_0-+3V3 -> Board_0-VIN_RAW
- FB2 pad 2: Board_4-+3V3 -> Board_4-VIN_RAW
- FB2 pad 2: Board_2-+3V3 -> Board_2-VIN_RAW
- FB2 pad 2: Board_1-+3V3 -> Board_1-VIN_RAW
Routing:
- net Board_0-SCL: track 28.5 -> 48.8 mm, vias 2 -> 3
- net Board_4-SCL: track 28.5 -> 48.8 mm, vias 2 -> 3
- net Board_1-SCL: track 28.5 -> 48.8 mm, vias 2 -> 3
- net Board_2-SCL: track 28.5 -> 48.8 mm, vias 2 -> 3
- net Board_3-SCL: track 28.5 -> 48.8 mm, vias 2 -> 3
- net Board_3-VIN_RAW: track 0.00 -> 19.8 mm, vias 0 -> 3
- net Board_4-VIN_RAW: track 0.00 -> 19.8 mm, vias 0 -> 3
- net Board_2-VIN_RAW: track 0.00 -> 19.8 mm, vias 0 -> 3
- net Board_1-VIN_RAW: track 0.00 -> 19.8 mm, vias 0 -> 3
- net Board_0-VIN_RAW: track 0.00 -> 19.8 mm, vias 0 -> 3
- net Board_3-MDI_CT: track 16.8 -> 8.32 mm
- net Board_2-MDI_CT: track 16.8 -> 8.32 mm
- net Board_1-MDI_CT: track 16.8 -> 8.32 mm
- net Board_0-MDI_CT: track 16.8 -> 8.32 mm
- net Board_4-MDI_CT: track 16.8 -> 8.32 mm
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- added copper zone on In2.Cu, net Board_0-GND
- added copper zone on In2.Cu, net Board_1-GND
- added copper zone on In2.Cu, net Board_2-GND
- added copper zone on In2.Cu, net Board_3-GND
- added copper zone on In2.Cu, net Board_4-GND
- removed copper zone on In2.Cu, net Board_0-+3V3
- removed copper zone on In2.Cu, net Board_1-+3V3
- removed copper zone on In2.Cu, net Board_2-+3V3
- removed copper zone on In2.Cu, net Board_3-+3V3
- removed copper zone on In2.Cu, net Board_4-+3V3
